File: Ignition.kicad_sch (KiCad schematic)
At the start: 0 parts

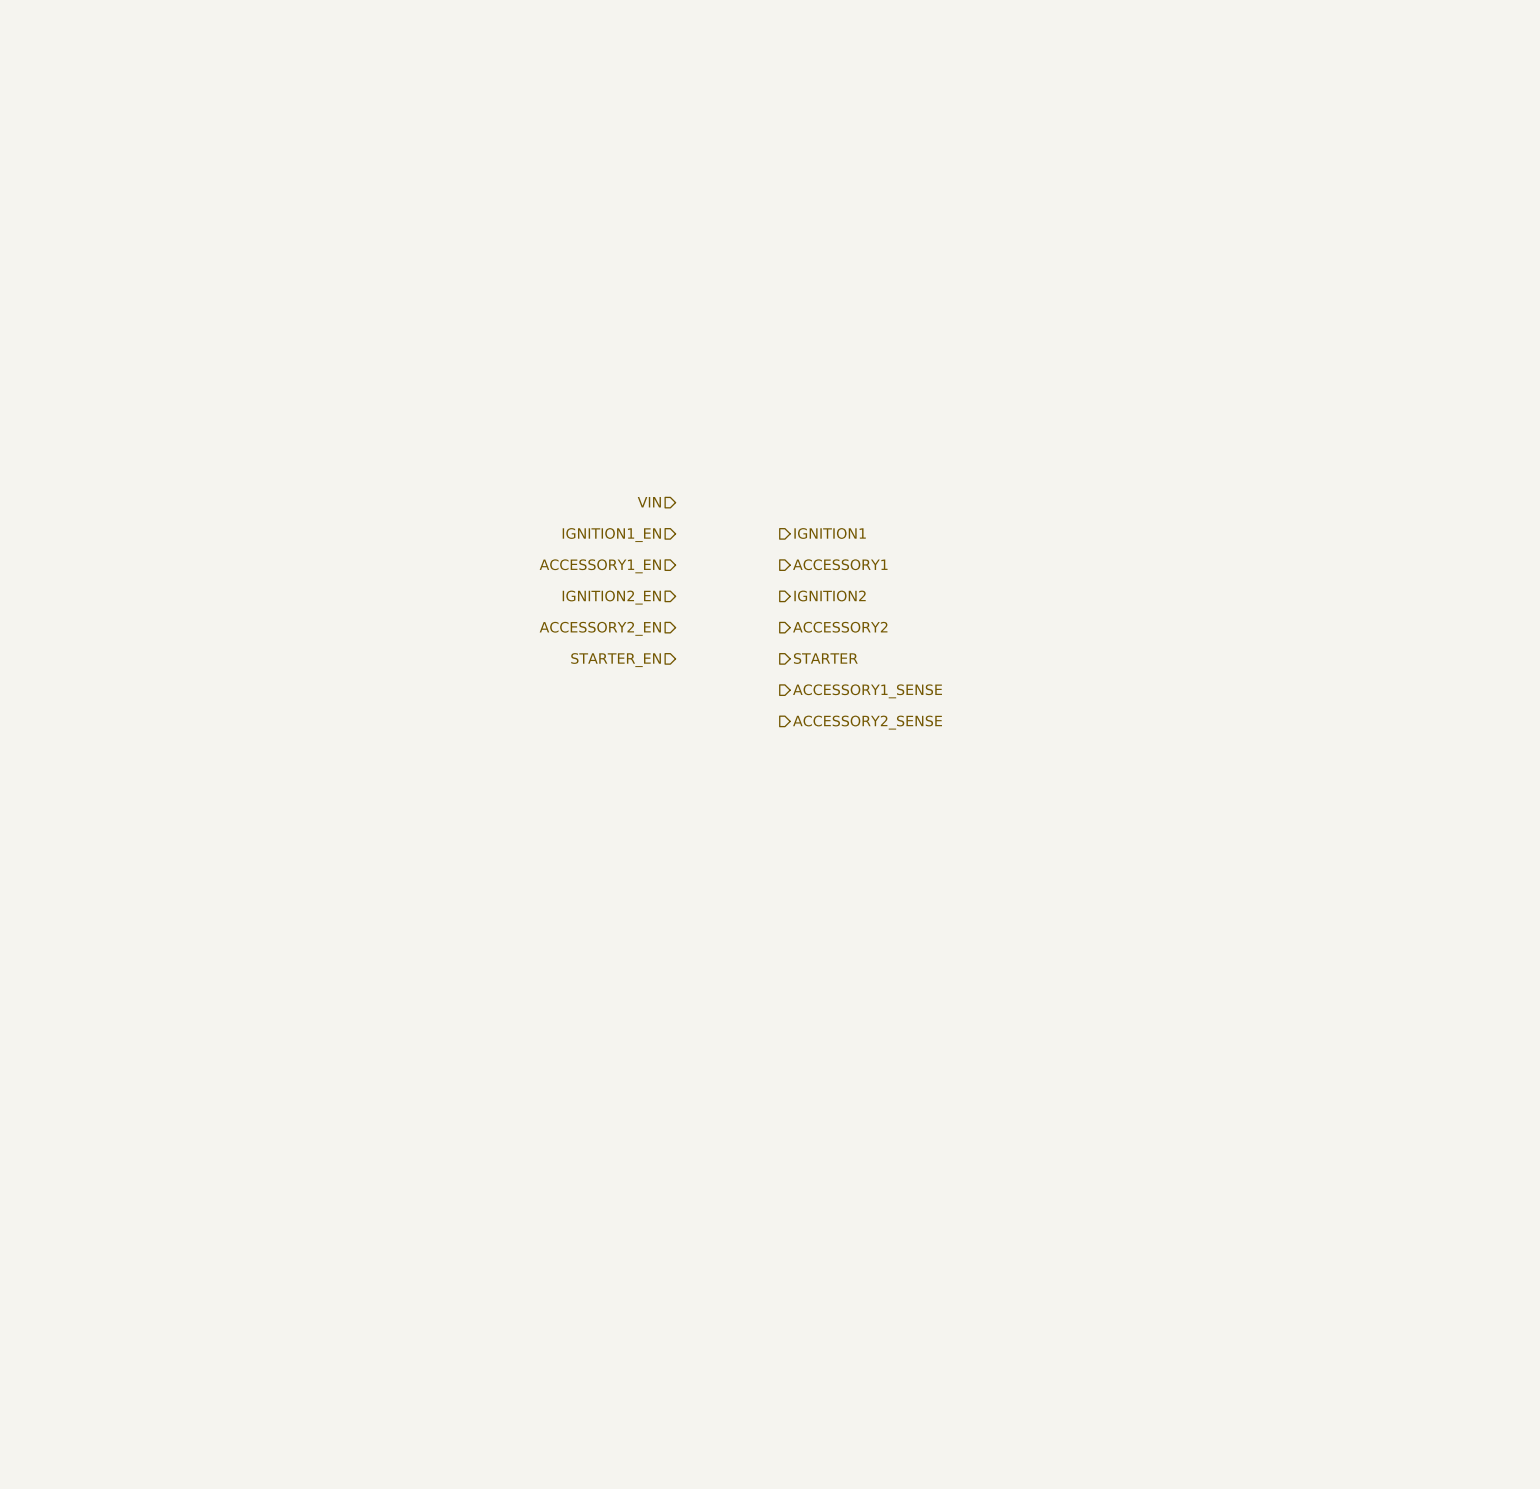
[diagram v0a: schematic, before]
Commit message: working on ignition and power output sheets
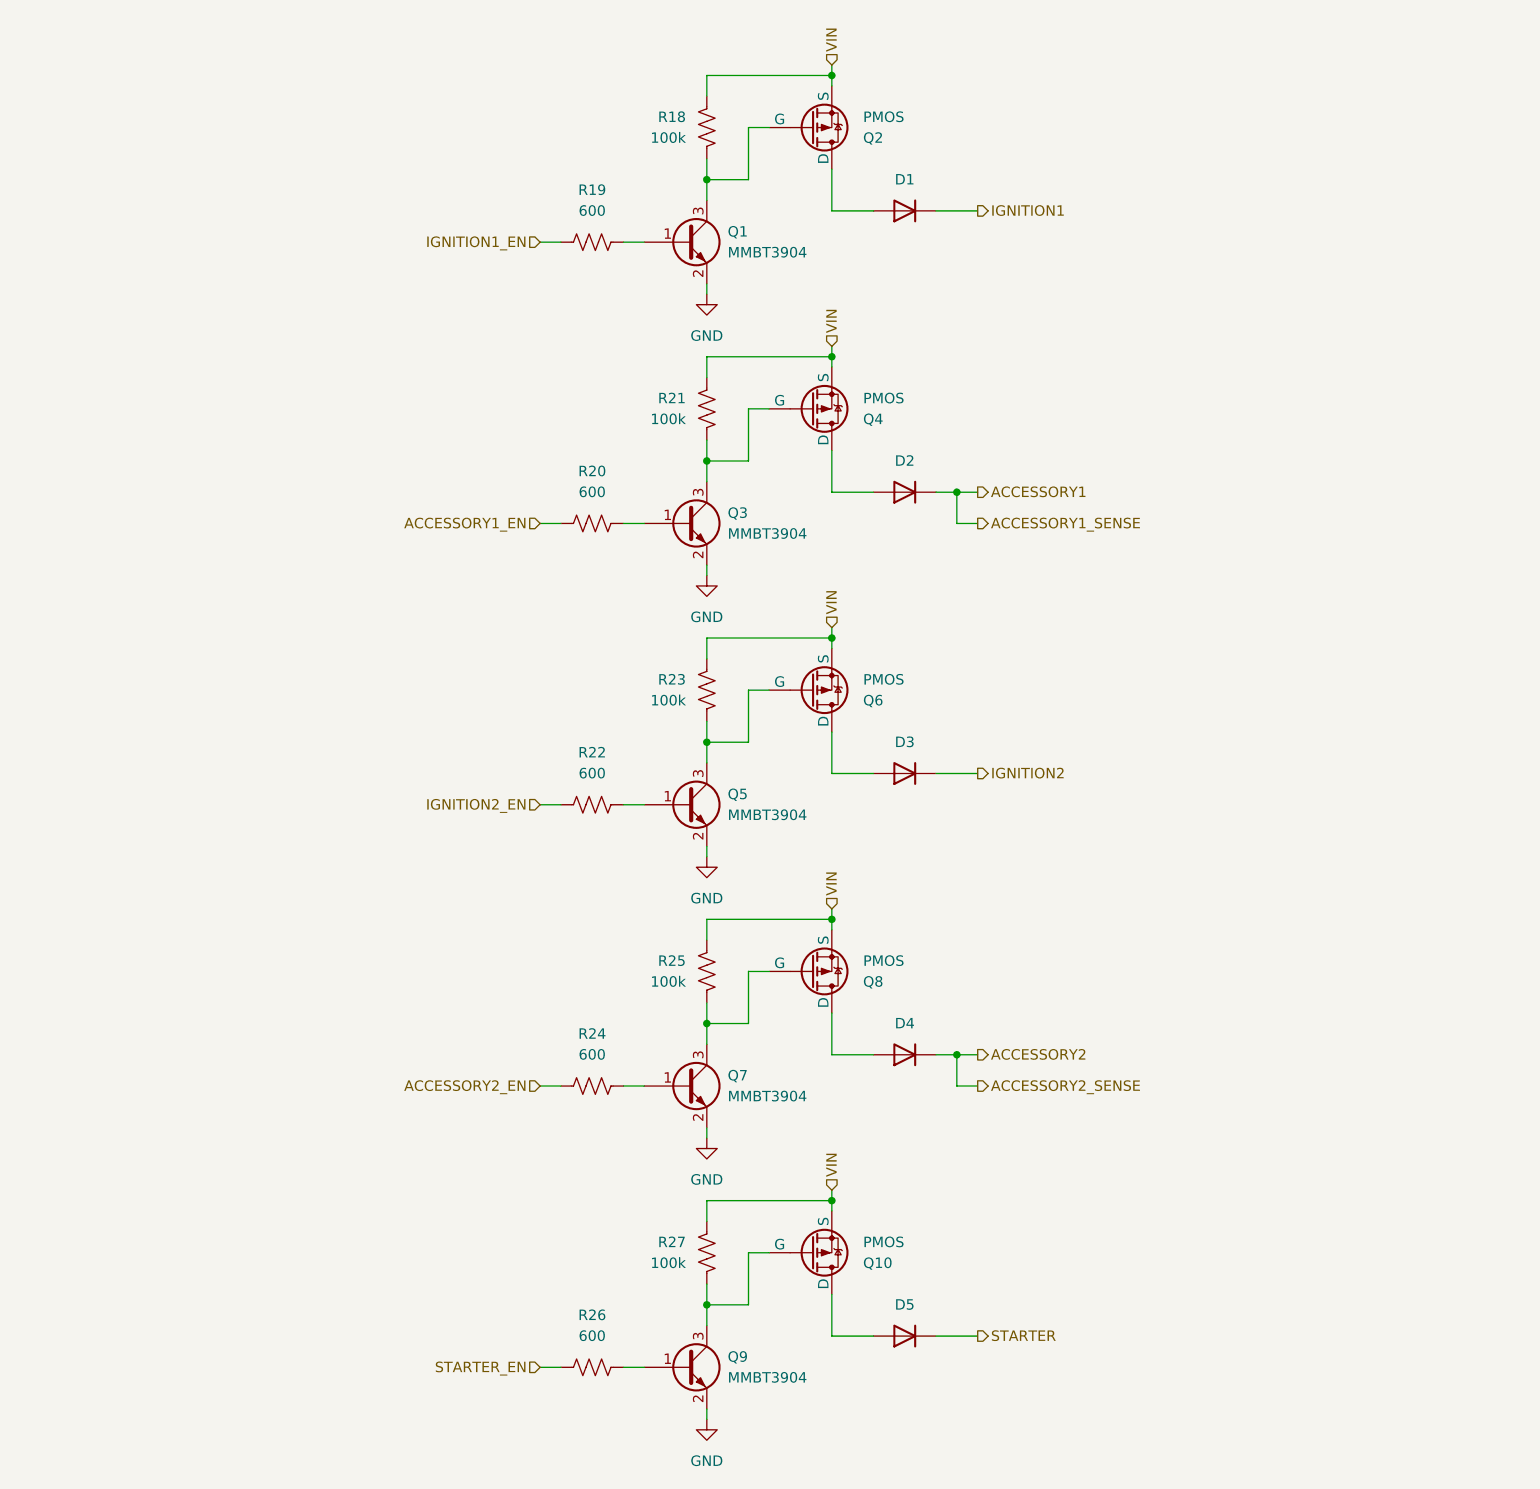
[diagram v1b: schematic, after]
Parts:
- added D1, D2, D3, D4, D5: D, symbol Simulation_SPICE:D
- added Q1, Q3, Q5, Q7, Q9: MMBT3904, Package_TO_SOT_SMD:SOT-23, symbol Transistor_BJT:MMBT3904
- added Q10, Q2, Q4, Q6, Q8: PMOS, symbol Simulation_SPICE:PMOS
- added R18, R21, R23, R25, R27: 100k, symbol Device:R_US
- added R19, R20, R22, R24, R26: 600, symbol Device:R_US
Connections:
- net ACCESSORY1: now also D2.1 (K)
- net ACCESSORY1_EN: now also R20.2
- net ACCESSORY2: now also D4.1 (K)
- net ACCESSORY2_EN: now also R24.2
- net IGNITION1: now also D1.1 (K)
- net IGNITION1_EN: now also R19.2
- net IGNITION2: now also D3.1 (K)
- net IGNITION2_EN: now also R22.2
- net STARTER: now also D5.1 (K)
- net STARTER_EN: now also R26.2
- net VIN: now also Q10.3 (S), Q2.3 (S), Q4.3 (S), Q6.3 (S), Q8.3 (S), R18.1, R21.1, R23.1, R25.1, R27.1
- new net: D1.2 (A), Q2.1 (D)
- new net: D5.2 (A), Q10.1 (D)
- new net: Q10.2 (G), Q9.3 (C), R27.2
- new net: Q7.3 (C), Q8.2 (G), R25.2
- new net: Q5.1 (B), R22.1
- new net: Q5.3 (C), Q6.2 (G), R23.2
- new net: Q1.1 (B), R19.1
- new net: D3.2 (A), Q6.1 (D)
- new net: Q9.1 (B), R26.1
- new net: Q1.3 (C), Q2.2 (G), R18.2
- new net: D2.2 (A), Q4.1 (D)
- new net: D4.2 (A), Q8.1 (D)
- new net: Q7.1 (B), R24.1
- new net: Q3.1 (B), R20.1
- new net: Q3.3 (C), Q4.2 (G), R21.2
- new net GND: Q1.2 (E), Q3.2 (E), Q5.2 (E), Q7.2 (E), Q9.2 (E)

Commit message: switch Ignition page to use load drivers rather than discrete FETs
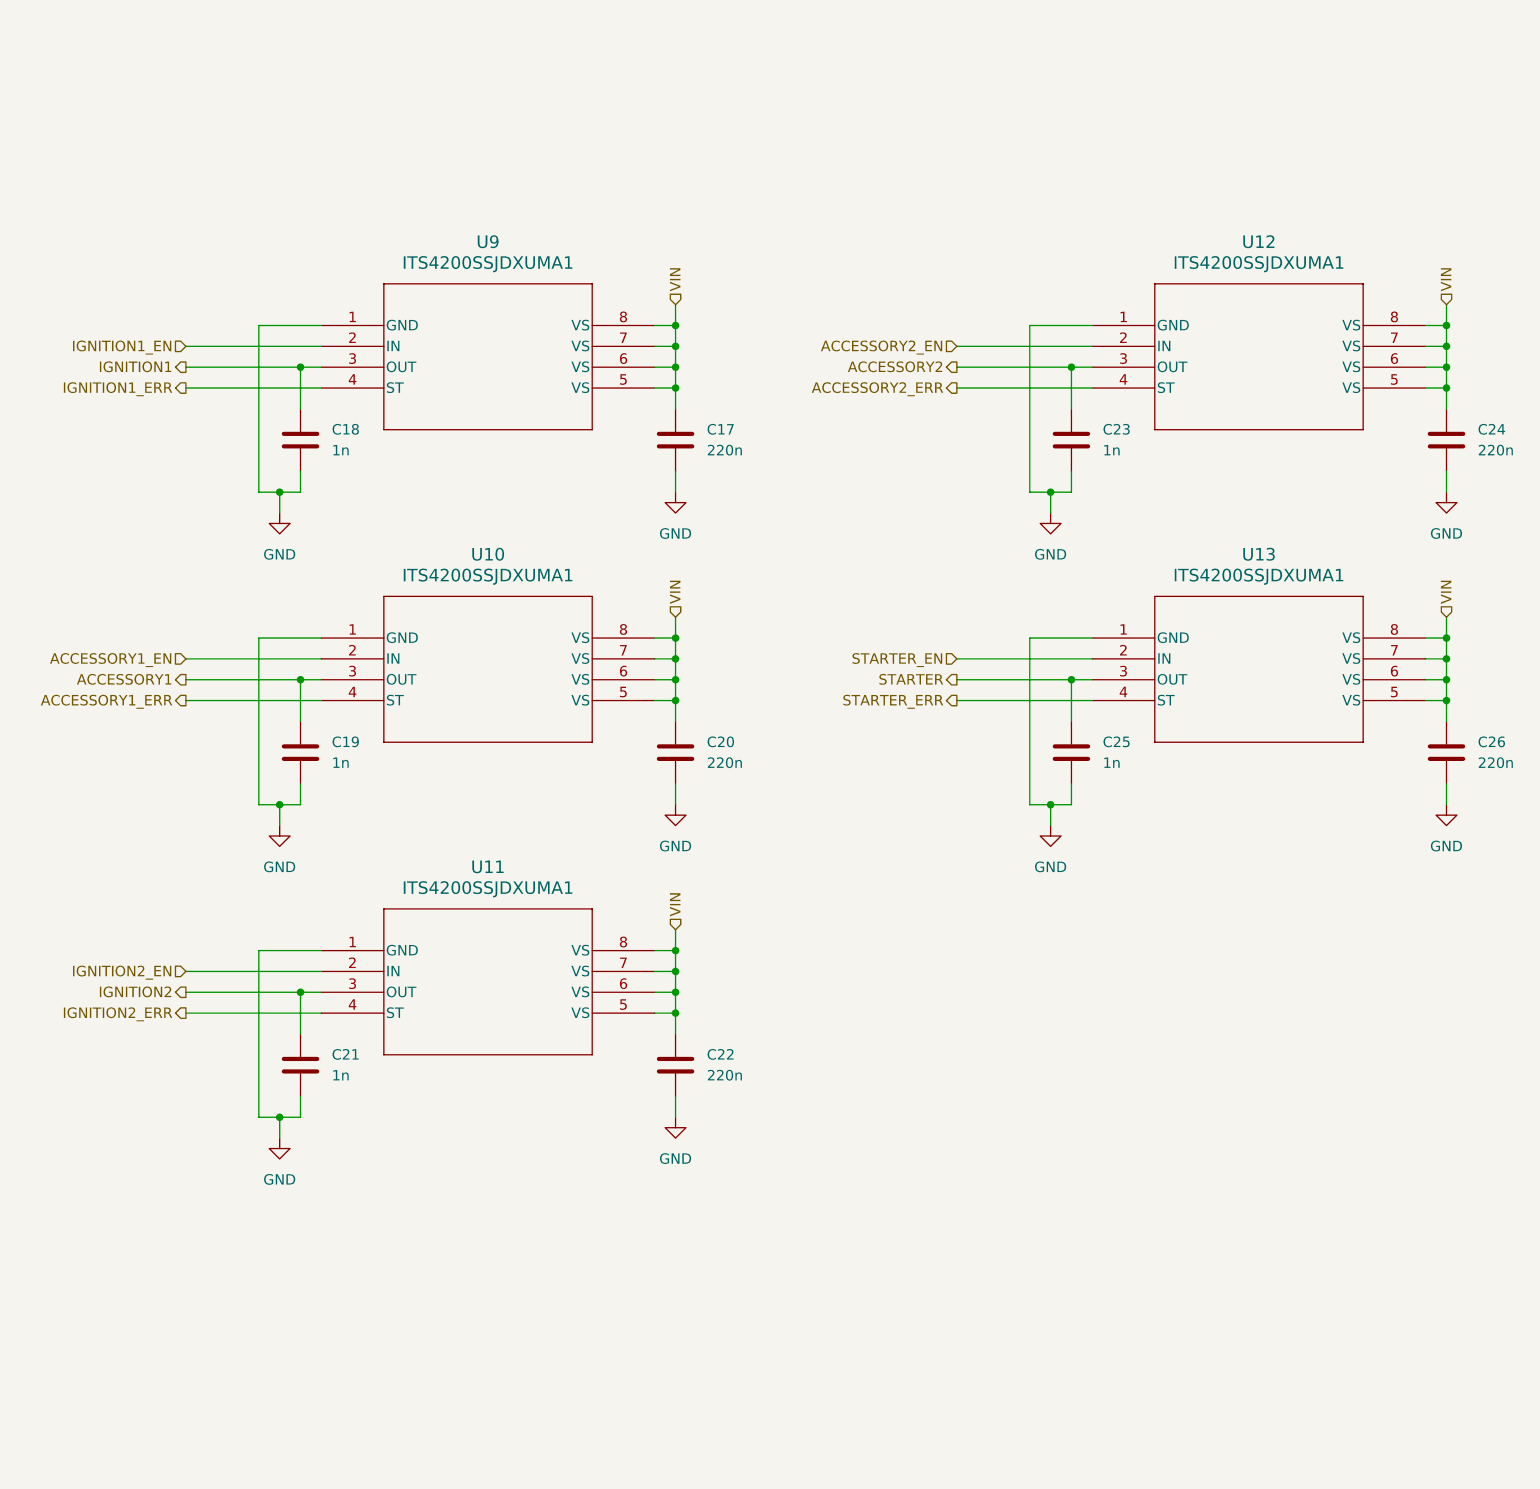
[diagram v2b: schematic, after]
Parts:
- removed D1, D2, D3, D4, D5: D, symbol Simulation_SPICE:D
- removed Q1, Q3, Q5, Q7, Q9: MMBT3904, Package_TO_SOT_SMD:SOT-23, symbol Transistor_BJT:MMBT3904
- removed Q10, Q2, Q4, Q6, Q8: PMOS, symbol Simulation_SPICE:PMOS
- removed R18, R21, R23, R25, R27: 100k, symbol Device:R_US
- removed R19, R20, R22, R24, R26: 600, symbol Device:R_US
- added C17, C20, C22, C24, C26: 220n, symbol Device:C
- added C18, C19, C21, C23, C25: 1n, symbol Device:C
- added U10, U11, U12, U13, U9: ITS4200SSJDXUMA1, PG-DSO-8-24_INF, symbol ITS4200SSJDXUMA1:ITS4200SSJDXUMA1
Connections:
- net ACCESSORY1: now also C19.2, U10.3 (OUT)
- net ACCESSORY1_EN: now also U10.2 (IN)
- net ACCESSORY2: now also C23.2, U12.3 (OUT)
- net ACCESSORY2_EN: now also U12.2 (IN)
- net GND: now also C17.1, C18.1, C19.1, C20.1, C21.1, C22.1, C23.1, C24.1, C25.1, C26.1, U10.1 (GND), U11.1 (GND), U12.1 (GND), U13.1 (GND), U9.1 (GND)
- net IGNITION1: now also C18.2, U9.3 (OUT)
- net IGNITION1_EN: now also U9.2 (IN)
- net IGNITION2: now also C21.2, U11.3 (OUT)
- net IGNITION2_EN: now also U11.2 (IN)
- net STARTER: now also C25.2, U13.3 (OUT)
- net STARTER_EN: now also U13.2 (IN)
- net VIN: now also C17.2, C20.2, C22.2, C24.2, C26.2, U10.5 (VS), U10.6 (VS), U10.7 (VS), U10.8 (VS), U11.5 (VS), U11.6 (VS), U11.7 (VS), U11.8 (VS), U12.5 (VS), U12.6 (VS), U12.7 (VS), U12.8 (VS), U13.5 (VS), U13.6 (VS), U13.7 (VS), U13.8 (VS), U9.5 (VS), U9.6 (VS), U9.7 (VS), U9.8 (VS)
- new net ACCESSORY1_ERR: U10.4 (ST)
- new net ACCESSORY2_ERR: U12.4 (ST)
- new net IGNITION1_ERR: U9.4 (ST)
- new net IGNITION2_ERR: U11.4 (ST)
- new net STARTER_ERR: U13.4 (ST)
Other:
- company: (none) -> J2B
